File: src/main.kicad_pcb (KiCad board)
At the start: 4 copper layers, 54 parts, among them P301 CONN_01X15, P302 CONN_01X03, P501 CONN_01X07, Q501 MMBT3904, Q502 MMBT3904, U301 LM741, U302 DG444, U303 LM741, U304 LM741, U305 LM311N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

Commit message: improve
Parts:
- moved R303 0.51 mm to (72.6, 72.6)
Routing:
- net Net-(C311-Pad1): track 88.7 -> 87.6 mm, vias 8 -> 6
- net Net-(P302-Pad2): track 34.8 -> 35.4 mm
- net IN_CTL: track 14.9 -> 15.4 mm, vias 1 -> 2
- net Net-(R303-Pad2): track 31.4 -> 30.9 mm

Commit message: update
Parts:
- moved C305 0.51 mm to (93.2, 85.1)
- moved C307 0.51 mm to (110.2, 84.8)
- moved C313 0.51 mm to (74.9, 85.1)
- moved R304 0.51 mm to (102.1, 90.7)
- moved R305 0.51 mm to (102.1, 95.5)
- moved U304 0.51 mm to (97.8, 85.1)
- moved U305 0.51 mm to (114.8, 84.8)
- moved C301 0.51 mm to (50.5, 66.5)
- moved C302 0.51 mm to (56.1, 78.0)
- moved C303 0.51 mm to (79.5, 85.1)
- moved C304 0.51 mm to (89.4, 85.1)
- moved C306 0.51 mm to (102.6, 85.1)
- moved C308 0.51 mm to (119.4, 84.8)
- moved C309 0.51 mm to (65.0, 84.8)
- moved C310 0.51 mm to (53.8, 66.5)
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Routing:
- net REF: track 192.0 -> 210.4 mm
- net 0V: track 76.4 -> 72.8 mm
- net -VE: track 49.8 -> 49.0 mm
- net TRIGGER: track 116.1 -> 116.9 mm

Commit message: move right
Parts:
- moved C303 1.02 mm to (80.5, 85.1)
- moved C304 1.02 mm to (90.4, 85.1)
- moved C306 1.02 mm to (103.6, 85.1)
- moved C308 1.02 mm to (120.4, 84.8)
- moved C309 1.02 mm to (66.0, 84.8)
- moved C311 1.02 mm to (84.8, 77.2)
- moved C312 1.02 mm to (56.6, 92.2)
- moved C314 1.02 mm to (86.6, 72.9)
- moved D301 1.02 mm to (108.5, 94.5)
- moved D302 1.02 mm to (108.5, 91.7)
- moved P302 1.02 mm to (94.0, 95.2)
- moved R301 1.02 mm to (70.4, 92.7)
- moved R302 1.02 mm to (70.4, 99.8)
- moved R303 1.02 mm to (74.2, 72.6)
- moved R306 1.02 mm to (115.3, 77.5)
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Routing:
- net REF_SUB_CTL: track 7.79 -> 9.82 mm
- net TRIGGER: track 116.9 -> 118.4 mm
- net 3.3V: track 17.8 -> 19.4 mm
- net IN: track 12.5 -> 14.0 mm
- net IN_CTL: track 15.4 -> 16.9 mm
- net RESET: track 18.5 -> 20.0 mm
- net REF_PLUS_CTL: track 17.7 -> 19.2 mm

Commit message: update
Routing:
- net REF: track 210.8 -> 189.7 mm
- net Net-(R302-Pad1): track 51.3 -> 45.8 mm
- net Net-(C311-Pad1): track 87.7 -> 86.3 mm, vias 6 -> 5
- net Net-(Q502-Pad2): track 72.4 -> 71.0 mm
- net Net-(R503-Pad2): track 33.1 -> 32.2 mm
- net IN_CTL: track 16.9 -> 16.2 mm
- net Net-(Q501-Pad2): track 48.9 -> 48.4 mm
- net Net-(D301-Pad2): track 41.3 -> 40.8 mm
- net REF_SUB_CTL: track 9.82 -> 9.31 mm
- net (no net): vias 1 -> 0

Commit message: update
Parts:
- moved Q502 3.81 mm to (130.6, 36.3)
- moved C502 3.81 mm to (131.8, 51.1)
- moved C503 3.81 mm to (52.1, 35.3)
- moved C504 3.81 mm to (64.5, 48.5)
- moved C505 3.81 mm to (135.6, 45.0)
- moved C508 3.81 mm to (126.2, 45.0)
- moved Q501 3.81 mm to (58.7, 35.3)
- moved R503 3.81 mm to (62.5, 37.3)
- moved R504 3.81 mm to (70.4, 35.1)
- moved R505 3.81 mm to (70.4, 49.0)
- moved R506 3.81 mm to (119.9, 34.0)
- moved R507 3.81 mm to (119.9, 39.6)
- moved R508 3.81 mm to (119.9, 51.3)
- moved R510 3.81 mm to (52.8, 41.7)
- moved RV502 3.81 mm to (116.8, 47.2)
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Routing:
- net REF: track 189.7 -> 193.3 mm
- net H-0V: track 72.0 -> 75.1 mm
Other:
- board text added: "+VE"
- board text added: "-VE"
- board text added: "0V"
- board text added: "3.3"
- board text added: "HEAT-0V"
- board text added: "IN"
- board text added: "IN-CTL"
- board text added: "REF"
- board text added: "REF+CTL"
- board text added: "REF-CTL"
- board text added: "RESET"
- board text added: "TRIGGER"
- board text added: "V-0.2"
- board text removed: "V-0.1"

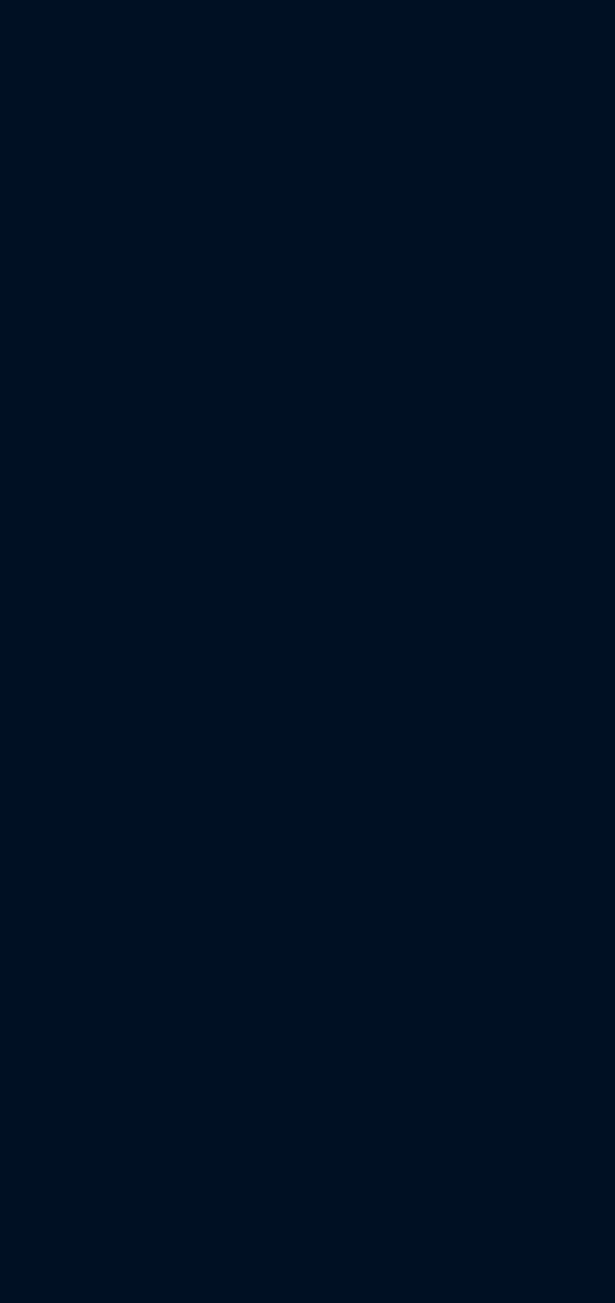
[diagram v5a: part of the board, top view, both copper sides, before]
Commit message: change pcb from 0V to AGND
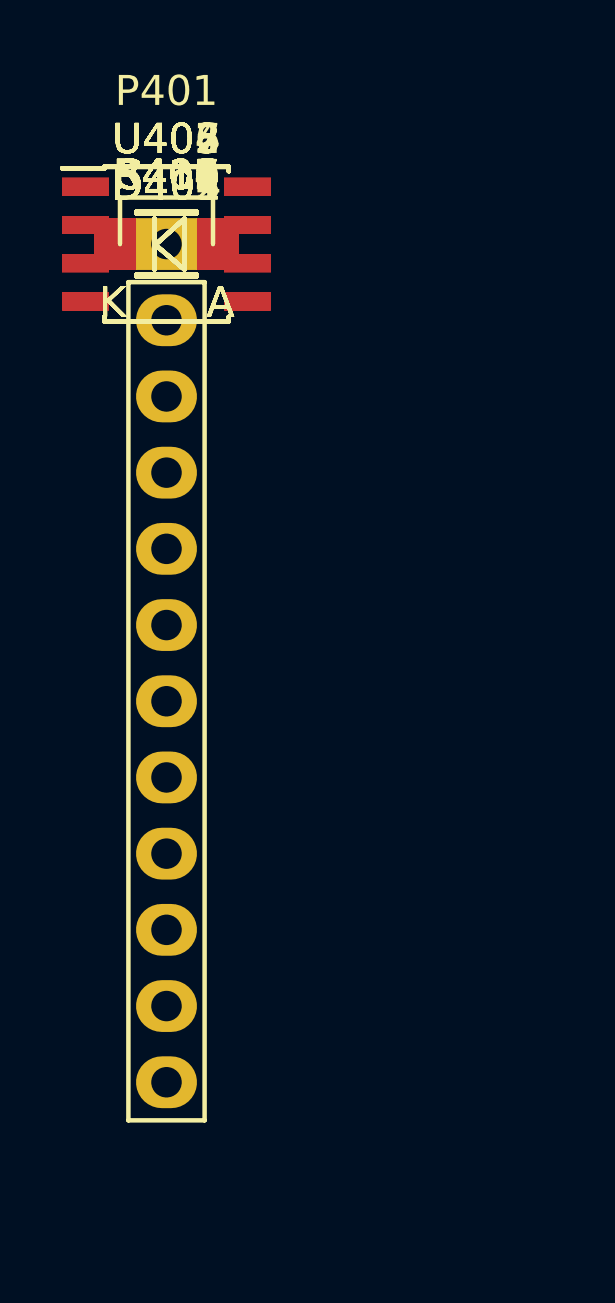
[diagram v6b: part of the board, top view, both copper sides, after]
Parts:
- added C401, C402, C403, C404, C405, C406, C407, C408, C409, C410, C411, C412: C, Capacitors_SMD:C_1206, F.Cu at (0.00, 0.00)
- added D401, D402, D403, D404: 1N4148, Diodes_SMD:MiniMELF_Standard, F.Cu at (0.00, 0.00)
- added P401: CONN_01X12, Pin_Headers:Pin_Header_Straight_1x12, F.Cu at (0.00, 0.00)
- added R404, R405, R406, R407, R408, R409, R410, R411, R412, R413, R414, R415, R416: R, Resistors_SMD:R_1206, F.Cu at (0.00, 0.00)
- added U402, U403, U404, U405, U406, U407: LM741, Housings_SOIC:SOIC-8_3.9x4.9mm_Pitch1.27mm, F.Cu at (0.00, 0.00)
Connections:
- net 0V renamed AGND
- net H-0V renamed H-GND

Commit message: initial clamps pcb
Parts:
- added R401: R, Resistors_SMD:R_1206, F.Cu at (6.00, -19.0)
- added R402: R, Resistors_SMD:R_1206, F.Cu at (6.00, -11.0)
- added R403: R, Resistors_SMD:R_1206, F.Cu at (-1.00, -9.00)
- added U401: DAC8734, Housings_QFP:TQFP-48_7x7mm_Pitch0.5mm, F.Cu at (-2.00, -18.0)
- moved D401 53.3 mm to (49.0, -21.0), turned to 90 degrees
- moved C410 50.6 mm to (46.0, -21.0), turned to 90 degrees
- moved D404 50.2 mm to (49.0, -11.0), turned to 90 degrees
- moved D403 49.8 mm to (49.0, 9.00), turned to 270 degrees
- moved D402 49.0 mm to (49.0, -1.00), turned to 90 degrees
- moved C406 47.3 mm to (46.0, -11.0), turned to 90 degrees
- moved C412 46.9 mm to (46.0, 9.00), turned to 90 degrees
- moved U404 46.1 mm to (41.0, -21.0), turned to 90 degrees
- moved C408 46.0 mm to (46.0, -1.00), turned to 90 degrees
- moved U405 42.4 mm to (41.0, -11.0), turned to 90 degrees
- moved U407 42.0 mm to (41.0, 9.00), turned to 90 degrees
- moved C411 41.7 mm to (36.0, -21.0), turned to 270 degrees
- moved U406 41.0 mm to (41.0, -1.00), turned to 90 degrees
- moved R408 38.0 mm to (31.0, -22.0), turned to 180 degrees
- moved C403 37.6 mm to (36.0, -11.0), turned to 270 degrees
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
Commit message: update before refactor
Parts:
- moved R416 42.6 mm to (48.0, -26.0), turned to 180 degrees
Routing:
- net AGND: track 72.6 -> 234.8 mm, vias 21 -> 33
- net OUT: track 0.00 -> 140.1 mm, vias 0 -> 2
- net +VE: track 69.7 -> 194.9 mm, vias 12 -> 21
- net -VE: track 48.8 -> 167.6 mm, vias 9 -> 17
- net 3.3V: track 19.1 -> 132.9 mm, vias 2 -> 3
- net REF: track 193.3 -> 286.8 mm
- net REF-CTL: track 0.00 -> 68.1 mm, vias 0 -> 1
- net I-FB: track 0.00 -> 58.1 mm
- net V-FB: track 0.00 -> 53.0 mm
- net Net-(R407-Pad1): track 0.00 -> 47.1 mm, vias 0 -> 2
- net V-SET: track 0.00 -> 30.1 mm, vias 0 -> 2
- net Net-(R406-Pad1): track 0.00 -> 26.2 mm, vias 0 -> 2
- net I-SET: track 0.00 -> 23.0 mm
- net Net-(R404-Pad1): track 0.00 -> 17.6 mm
- net Net-(R412-Pad1): track 0.00 -> 15.8 mm
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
